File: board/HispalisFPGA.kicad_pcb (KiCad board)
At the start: 4 copper layers, 91.3 x 79.9 mm, 134 parts, among them J1 HC-TYPE-C-16P-01A, Q1 DMG1012T, Q2 DMG1012T, Q3 DMG1012T, Q4 DMG1012T, SW1 SW_DIP_x08, U1 93LC46B, U2 FT2232HQ, Y1 12MHz

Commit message: Change switches
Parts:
- added SW2: MST22D18G2 125, HispalisFPGA:SW-SMD_MST22D18G2, F.Cu at (49.6, 139.2)
- added SW3: MST22D18G2 125, HispalisFPGA:SW-SMD_MST22D18G2, F.Cu at (59.6, 139.2)
- added SW4: MST22D18G2 125, HispalisFPGA:SW-SMD_MST22D18G2, F.Cu at (69.7, 139.2)
- added SW5: MST22D18G2 125, HispalisFPGA:SW-SMD_MST22D18G2, F.Cu at (79.7, 139.2)
- added SW6: MST22D18G2 125, HispalisFPGA:SW-SMD_MST22D18G2, F.Cu at (89.7, 139.2)
- added SW7: MST22D18G2 125, HispalisFPGA:SW-SMD_MST22D18G2, F.Cu at (99.7, 139.2)
- added SW8: MST22D18G2 125, HispalisFPGA:SW-SMD_MST22D18G2, F.Cu at (109.7, 139.2)
- SW1: value SW_DIP_x08 -> MST22D18G2 125; footprint Button_Switch_SMD:SW_DIP_SPSTx08_Slide_6.7x21.88mm_W6.73mm_P2.54mm_LowProfile_JPin -> HispalisFPGA:SW-SMD_MST22D18G2
- moved SW1 53.6 mm to (39.6, 139.2), turned to -90 degrees
- moved R16 47.6 mm to (37.3, 133.5)
- moved R17 40.3 mm to (46.3, 133.5)
- moved LD1 40.1 mm to (79.5, 126.4)
- moved LD2 39.2 mm to (83.5, 126.4)
- moved LD3 38.2 mm to (87.5, 126.4)
- moved LD4 37.2 mm to (91.5, 126.4)
- moved LD5 36.3 mm to (95.5, 126.4)
- moved LD6 35.3 mm to (99.5, 126.4)
- moved LD7 34.3 mm to (103.5, 126.4)
- moved LD8 33.4 mm to (107.5, 126.4)
- moved R18 32.8 mm to (57.3, 133.5)
- moved R19 25.7 mm to (66.3, 133.5)
- moved R20 18.6 mm to (77.3, 133.5)
- moved R21 11.4 mm to (86.3, 133.5)
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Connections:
- FPGA1 pad A10: LED7 -> SW7
- FPGA1 pad A11: LED5 -> SW5
- FPGA1 pad A12: LED3 -> SW3
- FPGA1 pad A13: LED1 -> SW1
- FPGA1 pad A3: SW7 -> LED7
- FPGA1 pad A4: SW5 -> LED5
- FPGA1 pad A5: SW3 -> LED3
- FPGA1 pad A6: SW1 -> LED1
- FPGA1 pad B10: LED8 -> SW8
- FPGA1 pad B11: LED6 -> SW6
- FPGA1 pad B12: LED4 -> SW4
- FPGA1 pad B13: LED2 -> SW2
- FPGA1 pad B3: SW8 -> LED8
- FPGA1 pad B4: SW6 -> LED6
- FPGA1 pad B5: SW4 -> LED4
- FPGA1 pad B6: SW2 -> LED2
- SW1 pad 1: +3V3 -> SW1
- SW1 pad 3: +3V3 -> unconnected-(SW1-C-Pad3)
- SW1 pad 4: +3V3 -> unconnected-(SW1-A-Pad4)
- SW1 pad 5: +3V3 -> unconnected-(SW1-B-Pad5)
- SW1 pad 6: +3V3 -> unconnected-(SW1-C-Pad6)
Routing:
- net +3V3: track 140.2 -> 249.7 mm
- net SW1: track 27.5 -> 64.0 mm
- net LED1: track 57.4 -> 20.9 mm
- net GND: track 272.0 -> 303.7 mm, vias 36 -> 35
- net LED2: track 53.6 -> 24.5 mm
- net SW2: track 31.2 -> 55.3 mm
- net LED3: track 47.9 -> 27.1 mm
- net SW8: track 44.2 -> 64.2 mm
- net LED8: track 31.0 -> 46.1 mm
- net SW3: track 31.8 -> 44.5 mm
- net SW7: track 40.9 -> 53.6 mm
- net LED4: track 44.1 -> 31.7 mm
- net LED7: track 29.6 -> 41.5 mm
- net SW6: track 40.0 -> 44.9 mm
- net LED6: track 34.6 -> 38.9 mm
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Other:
- board size 91.3 x 79.9 mm -> 91.3 x 85.3 mm
- board text removed: "SW1"
- board text removed: "SW2"
- board text removed: "SW3"
- board text removed: "SW4"
- board text removed: "SW5"
- board text removed: "SW6"
- board text removed: "SW7"
- board text removed: "SW8"

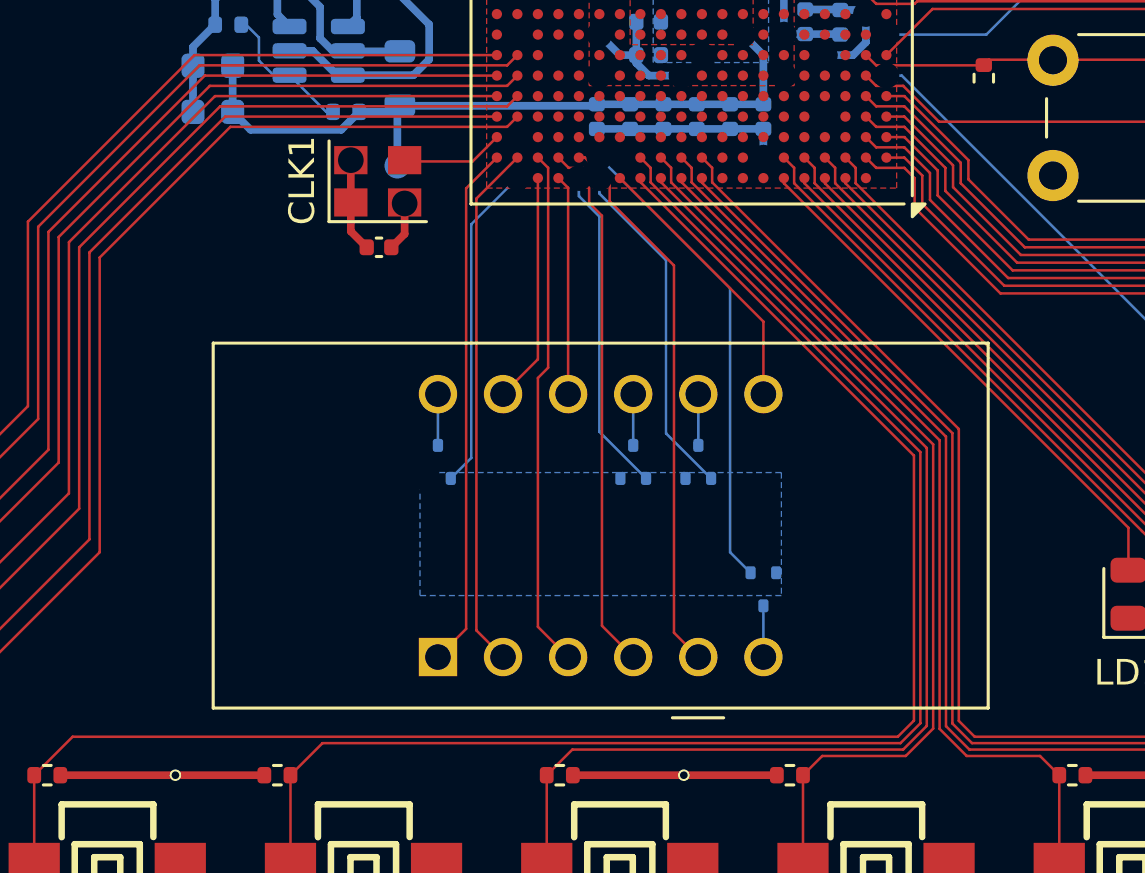
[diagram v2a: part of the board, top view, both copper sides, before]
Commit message: Set display symbol and footprint from EasyEDA
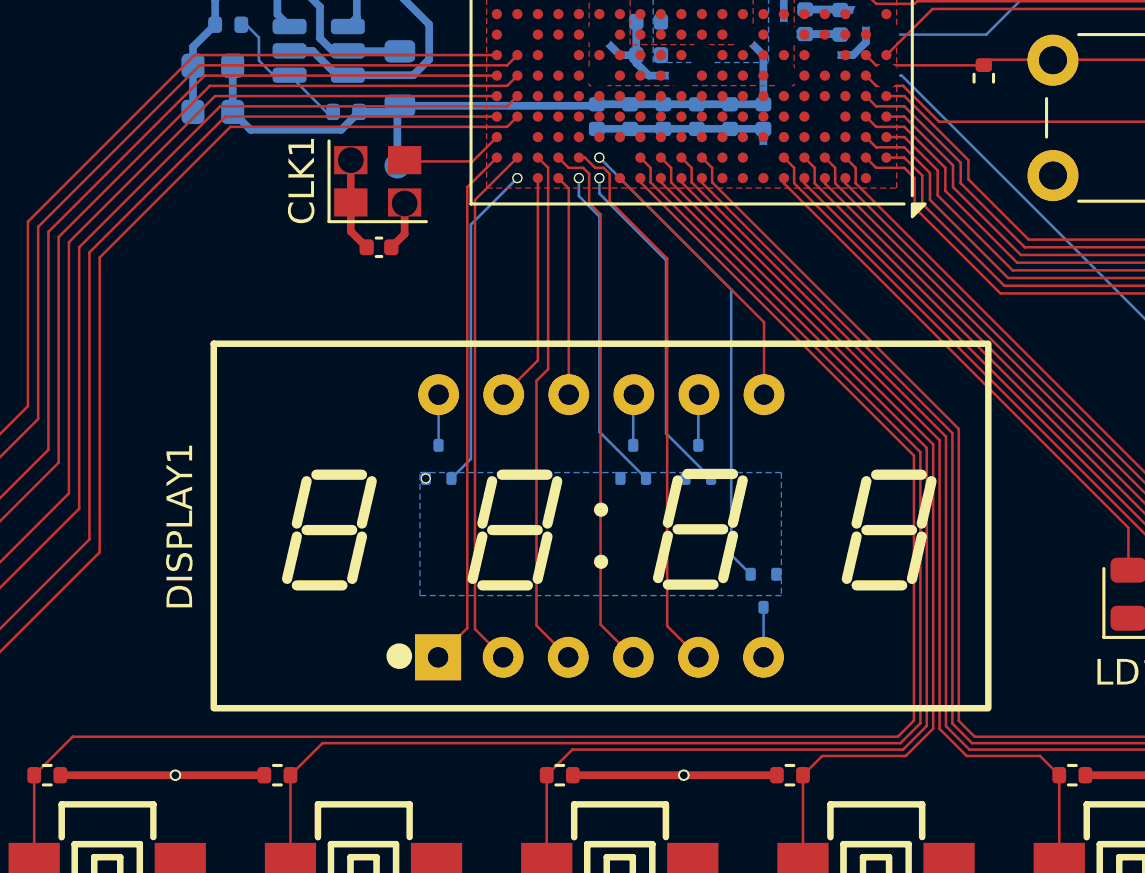
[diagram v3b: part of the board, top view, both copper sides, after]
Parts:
- DISPLAY1: footprint HispalisFPGA:MHDC3641SRBW -> HispalisFPGA:LED-SEG-TH_12P-L30.0-W14.0-P2.54-LS10.2
- moved Q4 13.7 mm to (65.3, 126.3), turned to -90 degrees
- moved Q1 13.6 mm to (52.6, 121.3), turned to 90 degrees
- moved DISPLAY1 6.36 mm to (58.9, 123.8), turned to 0 degrees
- moved Q2 2.54 mm to (60.2, 121.3)
- moved Q3 2.54 mm to (62.7, 121.3)
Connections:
- DISPLAY1 pad 12: Net-(DISPLAY1-CC1) -> Net-(DISPLAY1-DIG1)
- DISPLAY1 pad 6: Net-(DISPLAY1-CC4) -> Net-(DISPLAY1-DIG4)
- DISPLAY1 pad 8: Net-(DISPLAY1-CC3) -> Net-(DISPLAY1-DIG3)
- DISPLAY1 pad 9: Net-(DISPLAY1-CC2) -> Net-(DISPLAY1-DIG2)
- Q1 pad 1: DISPLAY_D4 -> DISPLAY_D1
- Q1 pad 3: Net-(DISPLAY1-CC4) -> Net-(DISPLAY1-DIG1)
- Q2 pad 1: DISPLAY_D3 -> DISPLAY_D2
- Q2 pad 3: Net-(DISPLAY1-CC3) -> Net-(DISPLAY1-DIG2)
- Q3 pad 1: DISPLAY_D2 -> DISPLAY_D3
- Q3 pad 3: Net-(DISPLAY1-CC2) -> Net-(DISPLAY1-DIG3)
- Q4 pad 1: DISPLAY_D1 -> DISPLAY_D4
- Q4 pad 3: Net-(DISPLAY1-CC1) -> Net-(DISPLAY1-DIG4)
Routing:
- net Net-(DISPLAY1-DIG3): track 0.00 -> 2.00 mm
- net Net-(DISPLAY1-DIG2): track 0.00 -> 2.00 mm
- net Net-(DISPLAY1-CC3): track 2.00 -> 0.00 mm
- net Net-(DISPLAY1-CC2): track 2.00 -> 0.00 mm
- net Net-(DISPLAY1-CC1): track 2.00 -> 0.00 mm
- net Net-(DISPLAY1-CC4): track 2.00 -> 0.00 mm
- net Net-(DISPLAY1-DIG1): track 0.00 -> 1.98 mm
- net Net-(DISPLAY1-DIG4): track 0.00 -> 1.95 mm

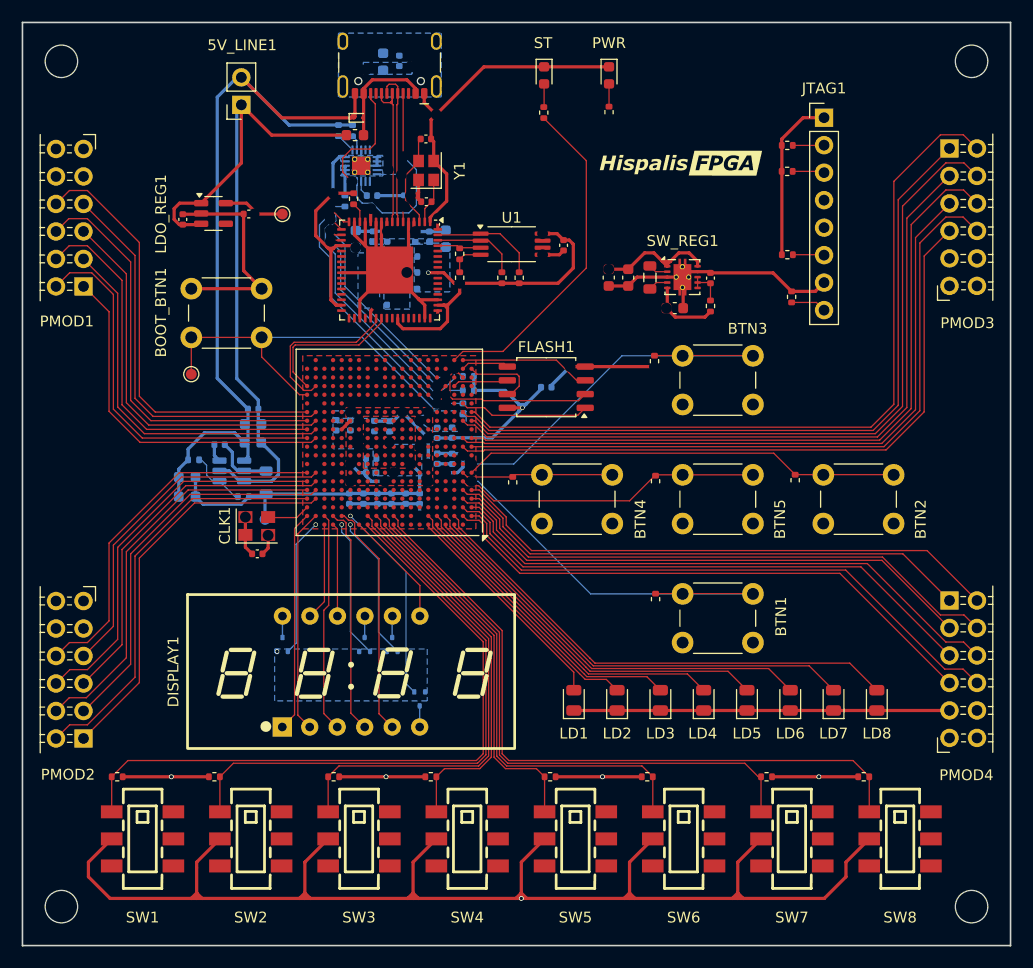
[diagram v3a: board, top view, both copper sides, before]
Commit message: Change LFE5U chip from BGA381 to BGA256 package
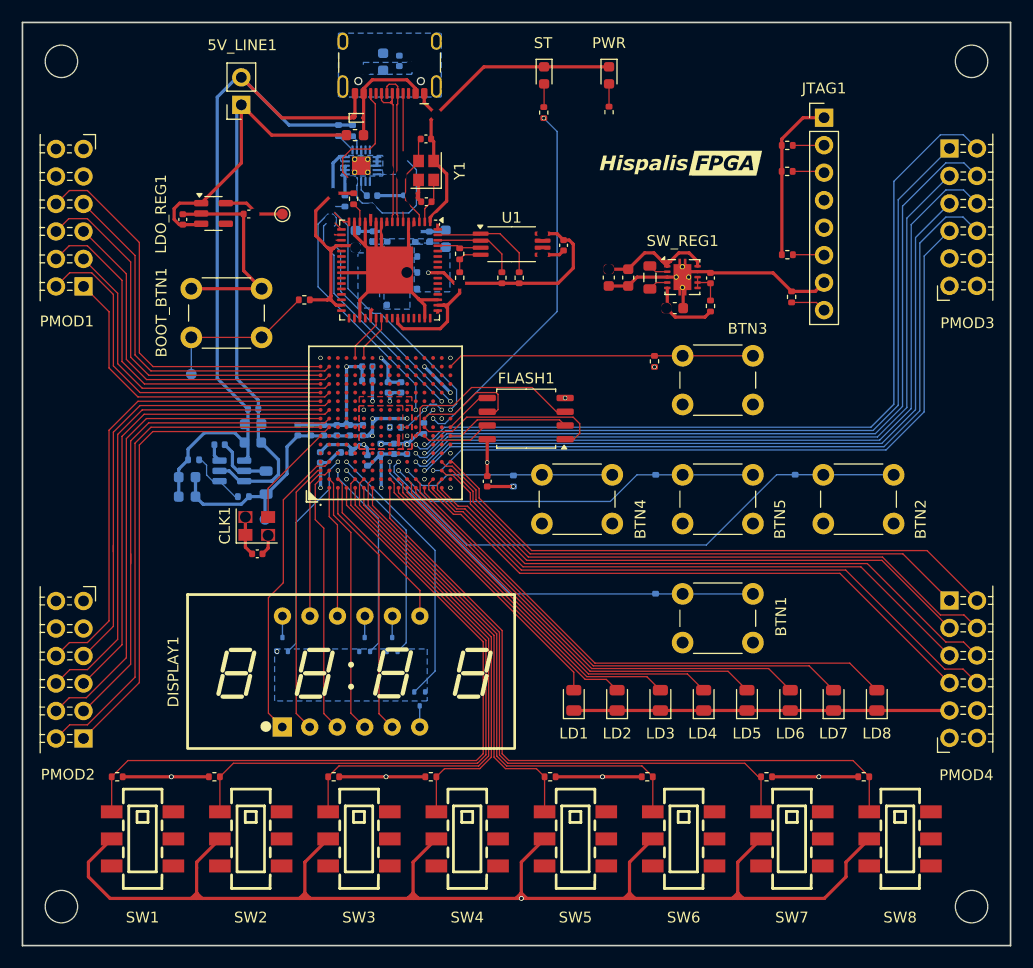
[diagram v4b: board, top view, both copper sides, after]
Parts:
- removed the C13 at (62.7, 107.8)
- removed the C18 at (60.1, 107.8)
- removed the C19 at (58.8, 107.8)
- removed the R31 at (69.8, 96.5)
- removed the R32 at (69.8, 97.8)
- added C10: 10nF, Capacitor_SMD:C_0402_1005Metric, B.Cu at (60.4, 95.6)
- added C14: 10nF, Capacitor_SMD:C_0402_1005Metric, B.Cu at (57.6, 101.5)
- added C16: 1nF, Capacitor_SMD:C_0402_1005Metric, B.Cu at (60.0, 101.5)
- added R29: 4.7K, Resistor_SMD:R_0402_1005Metric, B.Cu at (63.0, 101.2)
- added R34: 4.7K, Resistor_SMD:R_0402_1005Metric, B.Cu at (65.6, 101.3)
- C11, C37, C43: value 100nF -> 10nF
- C12, C38, C40, C9: value 10nF -> 100nF
- C15: value 10nF -> 1nF
- C45: moved to F.Cu
- FPGA1: value LFE5U-25F -> LFE5U-45F-7BG256I; footprint Package_BGA:Lattice_caBGA-381_17.0x17.0mm_Layout20x20_P0.8mm_Ball0.4mm_Pad0.4mm_NSMD -> HispalisFPGA:CABGA-256_L14.0-W14.0-R16-C16-P0.80-TL
- R24, R25, R27, R28, TP3: moved to B.Cu
- R33: value 4.7K -> 10K; moved to F.Cu
- moved R33 17.8 mm to (54.6, 89.4), turned to 180 degrees
- moved C11 11.9 mm to (55.2, 101.5), turned to 90 degrees
- moved C45 10.3 mm to (71.5, 106.2), turned to -90 degrees
- moved C12 9.85 mm to (56.4, 101.5), turned to 90 degrees
- moved C40 7.83 mm to (60.4, 104.3), turned to -90 degrees
- moved C15 6.82 mm to (58.8, 101.5), turned to 90 degrees
- moved C38 6.31 mm to (63.5, 97.5)
- moved C37 6.19 mm to (62.3, 97.5)
- moved C44 4.91 mm to (56.1, 104.0), turned to -90 degrees
- moved C41 4.67 mm to (58.5, 103.5), turned to 180 degrees
- moved C8 4.39 mm to (60.4, 96.9), turned to 180 degrees
- moved C39 4.10 mm to (62.9, 103.2), turned to -90 degrees
- moved C42 3.67 mm to (64.1, 103.2)
- moved C9 3.58 mm to (54.0, 101.5), turned to 90 degrees
- moved FLASH1 3.44 mm to (75.1, 100.4)
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- renumbered C10 to C13, C16 to C18, C14 to C19, R34 to R30, R29 to R31, R30 to R32
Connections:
- C9 pad 1: +2V5 -> +1V1
- FPGA1 pad A10: SW7 -> PMOD2_9
- FPGA1 pad A11: SW5 -> PMOD2_10
- FPGA1 pad A12: SW3 -> PMOD1_7
- FPGA1 pad A13: SW1 -> PMOD1_8
- FPGA1 pad A14: DISPLAY_SB -> PMOD1_9
- FPGA1 pad A15: DISPLAY_D3 -> PMOD1_10
- FPGA1 pad A16: DISPLAY_D2 -> GND
- FPGA1 pad A2: unconnected-(FPGA1G-PL35A-PadA2) -> DISPLAY_SDP
- FPGA1 pad A3: LED7 -> DISPLAY_SD
- FPGA1 pad A4: LED5 -> unconnected-(FPGA1A-PT6B-PadA4)
- FPGA1 pad A5: LED3 -> unconnected-(FPGA1A-PT18A-PadA5)
- FPGA1 pad A6: LED1 -> unconnected-(FPGA1A-PT18B-PadA6)
- FPGA1 pad A7: unconnected-(FPGA1B-PT18A-PadA7) -> CLK_16MHz
- FPGA1 pad A8: unconnected-(FPGA1B-PT18B-PadA8) -> PMOD2_7
- FPGA1 pad A9: unconnected-(FPGA1B-PT60A-PadA9) -> PMOD2_8
- FPGA1 pad B1: PMOD4_10 -> DISPLAY_SF
- FPGA1 pad B10: SW8 -> PMOD2_3
- FPGA1 pad B11: SW6 -> PMOD2_4
- FPGA1 pad B12: SW4 -> PMOD1_1
- FPGA1 pad B13: SW2 -> PMOD1_2
- FPGA1 pad B14: GND -> PMOD1_3
- FPGA1 pad B15: DISPLAY_D4 -> PMOD1_4
- FPGA1 pad B16: DISPLAY_SG -> unconnected-(FPGA1A-PR11A/URC_GPLL0T_IN-PadB16)
- FPGA1 pad B2: PMOD4_4 -> DISPLAY_SC
- FPGA1 pad B3: LED8 -> DISPLAY_SA
- FPGA1 pad B4: LED6 -> DISPLAY_SE
- FPGA1 pad B5: LED4 -> unconnected-(FPGA1A-PT15B-PadB5)
- FPGA1 pad B6: LED2 -> unconnected-(FPGA1A-PT31B-PadB6)
- FPGA1 pad B7: GND -> unconnected-(FPGA1A-PT36B/PCLKC0_1-PadB7)
- FPGA1 pad B8: unconnected-(FPGA1B-PT15B-PadB8) -> PMOD2_1
- FPGA1 pad B9: unconnected-(FPGA1B-PT58A-PadB9) -> PMOD2_2
- FPGA1 pad C1: PMOD4_9 -> DISPLAY_SG
- FPGA1 pad C2: PMOD4_3 -> DISPLAY_SB
- FPGA1 pad C3: unconnected-(FPGA1G-PL17C-PadC3) -> DISPLAY_D2
- FPGA1 pad C4: unconnected-(FPGA1G-PL14A-PadC4) -> DISPLAY_D1
- FPGA1 pad D1: PMOD4_8 -> SW1
- FPGA1 pad D15: unconnected-(FPGA1C-PT107A-PadD15) -> GND
- FPGA1 pad D2: PMOD4_2 -> GND
- FPGA1 pad D3: unconnected-(FPGA1G-PL17D-PadD3) -> DISPLAY_D3
- FPGA1 pad D4: GND -> DISPLAY_D4
- FPGA1 pad E1: PMOD4_7 -> SW3
- FPGA1 pad E16: unconnected-(FPGA1D-PR11C-PadE16) -> TXD_UART
- FPGA1 pad E2: PMOD4_1 -> SW2
- FPGA1 pad F1: BTN1 -> SW5
- FPGA1 pad F12: +3V3 -> unconnected-(FPGA1A-PR17D-PadF12)
- FPGA1 pad F13: GND -> unconnected-(FPGA1A-PR17C-PadF13)
- FPGA1 pad F14: GND -> unconnected-(FPGA1A-PR14D-PadF14)
- FPGA1 pad F15: +2V5 -> unconnected-(FPGA1A-PR20C-PadF15)
- FPGA1 pad F16: unconnected-(FPGA1D-PR11D-PadF16) -> RXD_UART
- FPGA1 pad F2: BTN5 -> SW4
- FPGA1 pad F6: +2V5 -> +3V3
- FPGA1 pad F7: GND -> +3V3
- FPGA1 pad F9: +3V3 -> GND
- FPGA1 pad G1: BTN2 -> SW7
- FPGA1 pad G11: GND -> +2V5
- FPGA1 pad G12: GND -> unconnected-(FPGA1A-PR20A-PadG12)
- FPGA1 pad G13: GND -> unconnected-(FPGA1A-PR20B-PadG13)
- FPGA1 pad G14: GND -> unconnected-(FPGA1A-PR23C/VREF1_2-PadG14)
- FPGA1 pad G15: GND -> unconnected-(FPGA1A-PR23B-PadG15)
- FPGA1 pad G2: BTN4 -> SW6
- FPGA1 pad G4: GND -> unconnected-(FPGA1B-PL20B-PadG4)
- FPGA1 pad G6: GND -> +1V1
- FPGA1 pad G7: GND -> +1V1
- FPGA1 pad G9: GND -> +1V1
- FPGA1 pad H1: BTN3 -> GND
- FPGA1 pad H10: +1V1 -> GND
- FPGA1 pad H11: +1V1 -> +3V3
- FPGA1 pad H12: +1V1 -> unconnected-(FPGA1A-PR26A-PadH12)
- FPGA1 pad H13: +1V1 -> unconnected-(FPGA1A-PR26B-PadH13)
- FPGA1 pad H14: +3V3 -> unconnected-(FPGA1A-PR23D-PadH14)
- FPGA1 pad H15: +3V3 -> unconnected-(FPGA1A-PR29B-PadH15)
- FPGA1 pad H16: unconnected-(FPGA1D-PR17D-PadH16) -> GND
- FPGA1 pad H8: +1V1 -> GND
- FPGA1 pad H9: +1V1 -> GND
- FPGA1 pad J1: unconnected-(FPGA1F-PL53B-PadJ1) -> SW8
- FPGA1 pad J11: GND -> +3V3
- FPGA1 pad J12: GND -> unconnected-(FPGA1A-PR26D-PadJ12)
- FPGA1 pad J13: +1V1 -> unconnected-(FPGA1A-PR26C-PadJ13)
- FPGA1 pad J14: GND -> unconnected-(FPGA1A-PR29C/GR_PCLK2_0-PadJ14)
- FPGA1 pad J15: +3V3 -> unconnected-(FPGA1A-PR32B/PCLKC2_1-PadJ15)
- FPGA1 pad J2: GND -> LED1
- FPGA1 pad J4: unconnected-(FPGA1F-PL50A-PadJ4) -> BTN1
- FPGA1 pad J7: GND -> +3V3
- FPGA1 pad J8: +1V1 -> GND
- FPGA1 pad K1: PMOD3_10 -> LED2
- FPGA1 pad K11: GND -> +3V3
- FPGA1 pad K12: GND -> unconnected-(FPGA1B-PR38B-PadK12)
- FPGA1 pad K13: +1V1 -> unconnected-(FPGA1B-PR38A/GR_PCLK3_0-PadK13)
- FPGA1 pad K14: GND -> unconnected-(FPGA1A-PR29D-PadK14)
- FPGA1 pad K15: GND -> unconnected-(FPGA1A-PR32D/PCLKC2_0-PadK15)
- FPGA1 pad K2: PMOD3_4 -> LED3
- FPGA1 pad K3: unconnected-(FPGA1F-PL50D-PadK3) -> BTN5
- FPGA1 pad K4: unconnected-(FPGA1F-PL56A-PadK4) -> BTN2
- FPGA1 pad K8: +1V1 -> GND
- FPGA1 pad L1: PMOD3_9 -> LED4
- FPGA1 pad L10: GND -> +1V1
- FPGA1 pad L11: GND -> +3V3
- FPGA1 pad L12: GND -> unconnected-(FPGA1B-PR38D-PadL12)
- FPGA1 pad L13: +1V1 -> unconnected-(FPGA1B-PR38C/GR_PCLK3_1-PadL13)
- FPGA1 pad L14: +3V3 -> unconnected-(FPGA1B-PR41C-PadL14)
- FPGA1 pad L15: +3V3 -> unconnected-(FPGA1B-PR35B/PCLKC3_1-PadL15)
- FPGA1 pad L2: PMOD3_3 -> LED5
- FPGA1 pad L3: unconnected-(FPGA1F-PL86C-PadL3) -> BTN4
- FPGA1 pad L7: +3V3 -> +2V5
- FPGA1 pad L9: GND -> +1V1
- FPGA1 pad M1: unconnected-(FPGA1F-PL89B-PadM1) -> LED6
- FPGA1 pad M10: GND -> TDO
- FPGA1 pad M11: GND -> unconnected-(FPGA1B-PR68A-PadM11)
- FPGA1 pad M12: GND -> unconnected-(FPGA1B-PR65C-PadM12)
- FPGA1 pad M13: +1V1 -> unconnected-(FPGA1B-PR44C-PadM13)
- FPGA1 pad M14: GND -> unconnected-(FPGA1B-PR41D-PadM14)
- FPGA1 pad M15: +3V3 -> unconnected-(FPGA1B-PR35D/PCLKC3_0-PadM15)
- FPGA1 pad M16: GND -> unconnected-(FPGA1B-PR35C/PCLKT3_0-PadM16)
- FPGA1 pad M2: GND -> LED7
- FPGA1 pad M4: unconnected-(FPGA1F-PL83A-PadM4) -> PMOD3_3
- FPGA1 pad M5: unconnected-(FPGA1F-PL77A-PadM5) -> PMOD3_2
- FPGA1 pad M6: +3V3 -> PMOD3_1
- FPGA1 pad M7: GND -> IO2
- FPGA1 pad M8: +1V1 -> unconnected-(FPGA1B-PB15B/DOUT/CSON-PadM8)
- FPGA1 pad M9: GND -> unconnected-(FPGA1B-PB18A/WRITEN-PadM9)
- FPGA1 pad N1: PMOD3_8 -> LED8
- FPGA1 pad N10: +1V1 -> CFG_0
- FPGA1 pad N11: +1V1 -> unconnected-(FPGA1B-PR68B-PadN11)
- FPGA1 pad N12: +1V1 -> unconnected-(FPGA1B-PR65D-PadN12)
- FPGA1 pad N13: +1V1 -> unconnected-(FPGA1B-PR59A-PadN13)
- FPGA1 pad N14: GND -> unconnected-(FPGA1B-PR44D-PadN14)
- FPGA1 pad N2: PMOD3_2 -> GND
- FPGA1 pad N3: unconnected-(FPGA1F-PL86A-PadN3) -> PMOD3_10
- FPGA1 pad N4: unconnected-(FPGA1F-PL83C-PadN4) -> PMOD3_9
- FPGA1 pad N5: unconnected-(FPGA1F-PL83B-PadN5) -> PMOD3_8
- FPGA1 pad N6: GND -> PMOD3_7
- FPGA1 pad N7: GND -> IO3
- FPGA1 pad N8: +1V1 -> CSSPIN
- FPGA1 pad N9: +1V1 -> SCK
- FPGA1 pad P1: PMOD3_7 -> PMOD4_10
- FPGA1 pad P10: +3V3 -> CFG_1
- FPGA1 pad P11: GND -> unconnected-(FPGA1B-PR68C/LRC_GPLL0T_IN-PadP11)
- FPGA1 pad P12: GND -> unconnected-(FPGA1B-PR68D/LRC_GPLL0C_IN-PadP12)
- FPGA1 pad P13: GND -> unconnected-(FPGA1B-PR62A-PadP13)
- FPGA1 pad P14: GND -> unconnected-(FPGA1B-PR59B-PadP14)
- FPGA1 pad P15: +2V5 -> unconnected-(FPGA1B-PR41B-PadP15)
- FPGA1 pad P2: PMOD3_1 -> PMOD4_4
- FPGA1 pad P3: unconnected-(FPGA1F-PL92C-PadP3) -> PMOD3_4
- FPGA1 pad P6: +2V5 -> unconnected-(FPGA1B-PL68C/LLC_GPLL0T_IN-PadP6)
- FPGA1 pad P7: GND -> unconnected-(FPGA1B-PB6B/D4/MOSI2/IO4-PadP7)
- FPGA1 pad P8: GND -> unconnected-(FPGA1B-PB13B/CS1N-PadP8)
- FPGA1 pad P9: +3V3 -> DONE
- FPGA1 pad R1: unconnected-(FPGA1H-PB4A-PadR1) -> PMOD4_9
- FPGA1 pad R2: CSSPIN -> PMOD4_3
- FPGA1 pad R3: unconnected-(FPGA1H-PB15B-PadR3) -> PMOD4_2
- FPGA1 pad R4: Net-(FPGA1I-CFG_0) -> PMOD4_1
- FPGA1 pad R5: TDI -> unconnected-(FPGA1B-PL65A-PadR5)
- FPGA1 pad T1: unconnected-(FPGA1H-PB4B-PadT1) -> GND
- FPGA1 pad T10: GND -> TCK
- FPGA1 pad T11: GND -> TMS
- FPGA1 pad T13: GND -> unconnected-(FPGA1B-PR65B-PadT13)
- FPGA1 pad T14: GND -> unconnected-(FPGA1B-PR62D-PadT14)
- FPGA1 pad T15: GND -> BTN3
- FPGA1 pad T16: unconnected-(FPGA1E-PR77A-PadT16) -> GND
- FPGA1 pad T3: unconnected-(FPGA1H-PB18A-PadT3) -> PMOD4_8
- FPGA1 pad T4: Net-(FPGA1I-CFG_1) -> PMOD4_7
- FPGA1 pad T5: TCK -> GND
- FPGA1 pad T6: GND -> unconnected-(FPGA1B-PB4A/D7/IO7-PadT6)
- FPGA1 pad T7: GND -> MISO
- FPGA1 pad T8: GND -> MOSI
- FPGA1 pad T9: GND -> unconnected-(FPGA1B-INITN-PadT9)
- R31 pad 1: Net-(FPGA1I-DONE) -> DONE
- R33 pad 1: Net-(FPGA1I-CFG_0) -> +3V3
- R33 pad 2: GND -> PROGRAMN
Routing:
- net DONE: track 0.00 -> 34.3 mm, vias 0 -> 2
- net Net-(FPGA1I-DONE): track 31.2 -> 0.00 mm
- net +3V3: track 249.7 -> 229.7 mm, vias 16 -> 15
- net +2V5: track 52.7 -> 35.4 mm, vias 5 -> 3
- net GND: track 303.7 -> 316.6 mm, vias 35 -> 31
- net BTN2: track 40.6 -> 52.8 mm, vias 0 -> 1
- net TDO: track 76.8 -> 88.0 mm
- net PMOD2_2: track 35.9 -> 46.9 mm
- net BTN3: track 39.3 -> 28.4 mm, vias 1 -> 0
- net PMOD2_4: track 32.9 -> 43.6 mm
- net TXD_UART: track 15.1 -> 4.47 mm
- net PMOD2_3: track 34.4 -> 44.5 mm
- net PMOD2_1: track 37.4 -> 47.5 mm
- net PMOD2_8: track 37.4 -> 47.5 mm
- net PMOD2_9: track 35.9 -> 46.0 mm
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- removed copper zone on B.Cu, net +2V5
